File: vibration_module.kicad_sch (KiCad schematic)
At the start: 22 parts, among them J1 I2C/PWR, U1 AT42QT1011-TSHR, U2 DRV2605LDGS, U3 STM32G031G8Ux, U4 TPS7A20xxxDQN

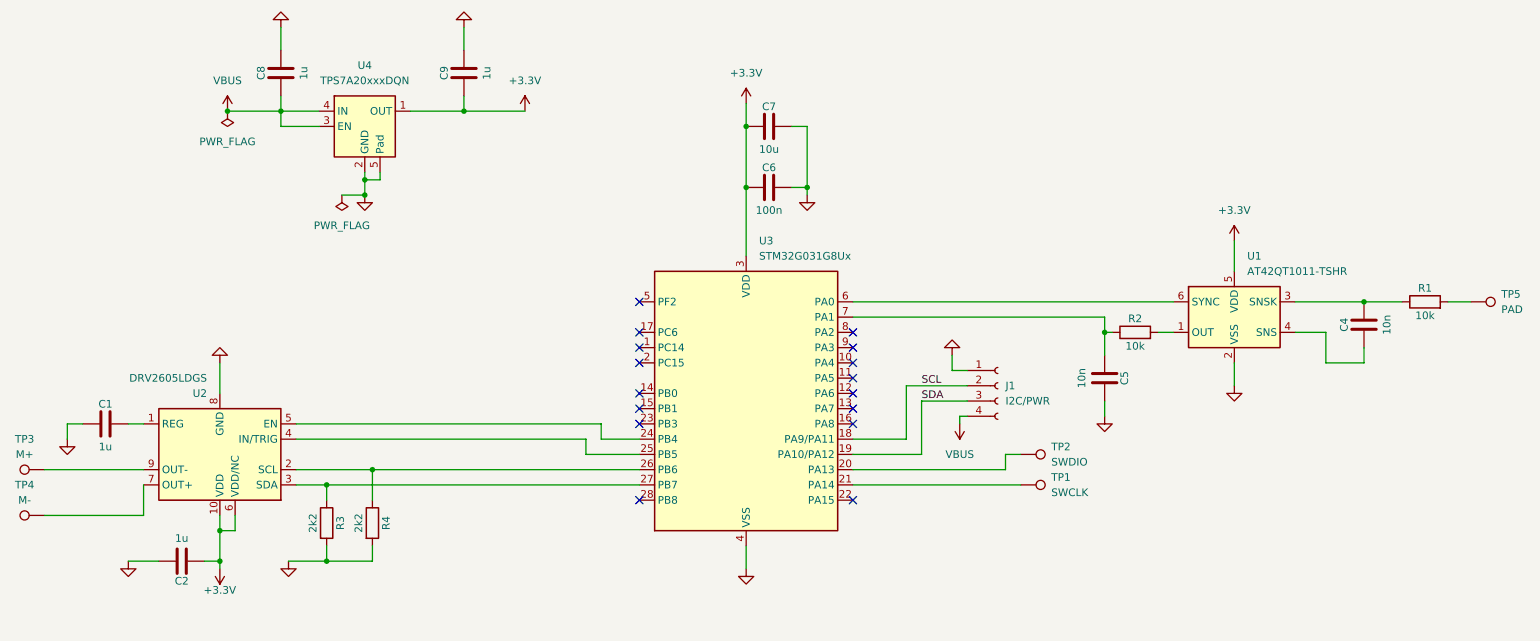
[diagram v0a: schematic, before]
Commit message: mouse switch integration
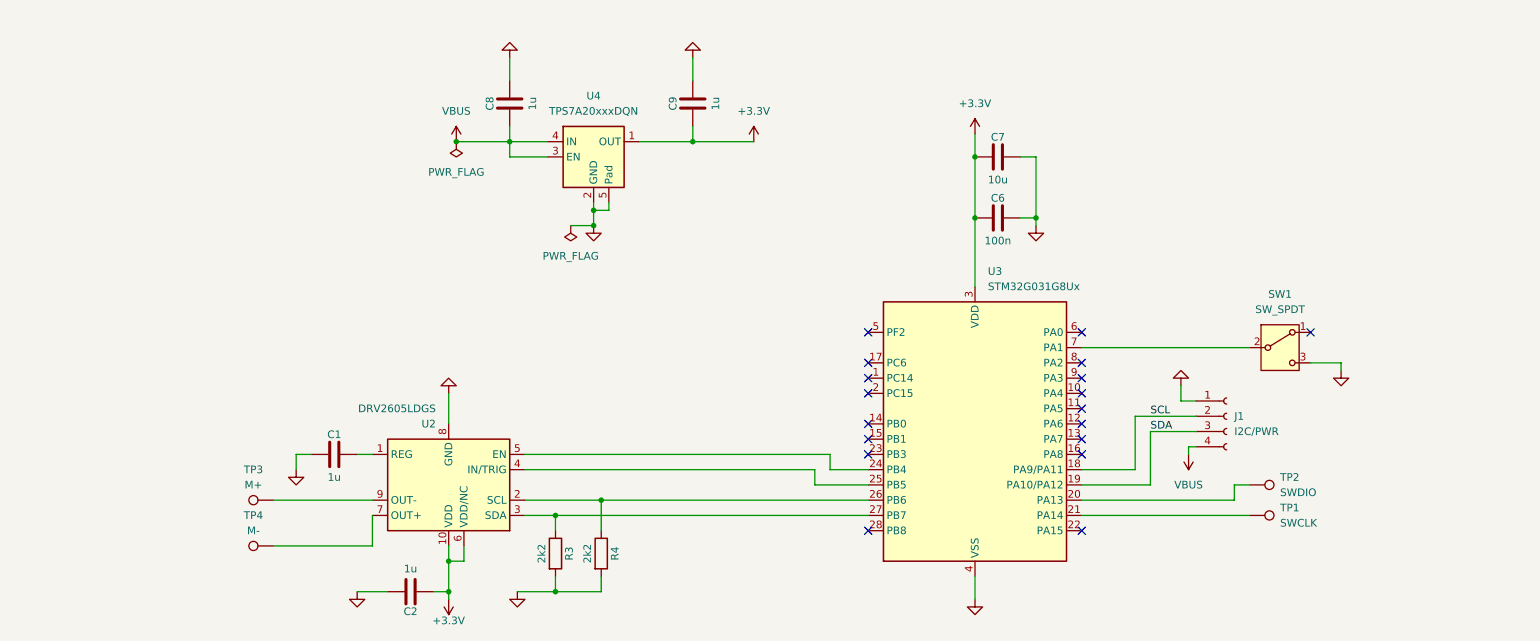
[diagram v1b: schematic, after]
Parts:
- removed C4, C5: 10n, Capacitor_SMD:C_0402_1005Metric, symbol Device:C
- removed R1, R2: 10k, Resistor_SMD:R_0402_1005Metric, symbol Device:R
- removed TP5: PAD, symbol Connector:TestPoint
- removed U1: AT42QT1011-TSHR, Package_TO_SOT_SMD:SOT-23-6, symbol Sensor_Touch:AT42QT1011-TSHR
- added SW1: SW_SPDT, Button_Switch_THT:SW_XKB_DM1-16UP-1, symbol Switch:SW_SPDT
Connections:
- net GND: now also SW1.3 (C)
- net at U3.7 (PA1): now also SW1.2 (B)
- no-connect marks 16 -> 18
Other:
- moved on the sheet: C1, C2, C6, C7, C8, C9, J1, R3, R4, TP1, TP2, TP3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

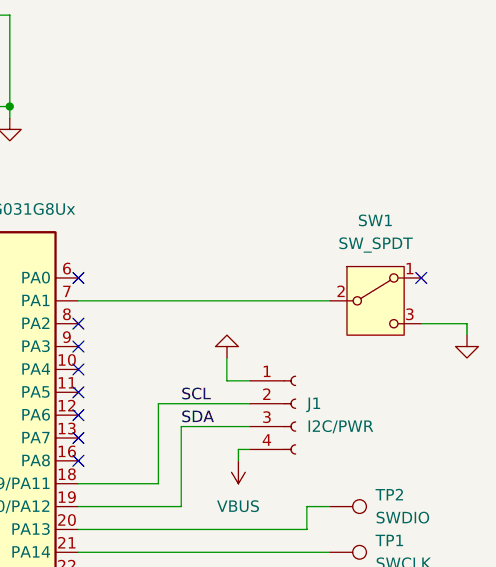
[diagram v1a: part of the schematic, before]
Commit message: keyboard version poc
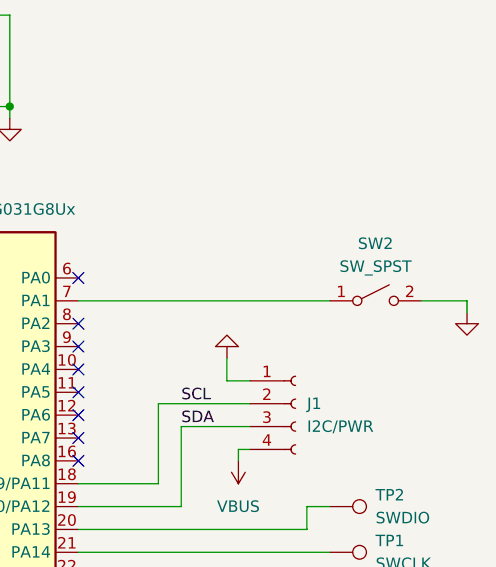
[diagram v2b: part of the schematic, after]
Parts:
- removed SW1: SW_SPDT, Button_Switch_THT:SW_XKB_DM1-16UP-1, symbol Switch:SW_SPDT
- added SW2: SW_SPST, PCM_Switch_Keyboard_Kailh:SW_Kailh_Choc_V1_1.00u, symbol Switch:SW_SPST
- J1: footprint Connector_Molex:Molex_PicoBlade_53048-0410_1x04_P1.25mm_Horizontal -> Connector_Molex:Molex_PicoBlade_53261-0471_1x04-1MP_P1.25mm_Horizontal
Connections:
- net GND: now also SW2.2 (B)
- net at U3.7 (PA1): now also SW2.1 (A)
- no-connect marks 18 -> 17
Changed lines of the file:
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@@
-	)
-	(no_connect
-		(at 240.03 101.6)
 	)
 	(no_connect
@@
 	(wire
 		(pts
-			(xy 240.03 106.68) (xy 245.11 106.68)
+			(xy 240.03 104.14) (xy 245.11 104.14)
 		)
 		(stroke
@@
 	(wire
 		(pts
-			(xy 245.11 106.68) (xy 245.11 107.95)
+			(xy 245.11 104.14) (xy 245.11 105.41)
 		)
 		(stroke
@@
 	)
 	(symbol
-		(lib_id "Switch:SW_SPDT")
-		(at 234.95 104.14 0)
-		(unit 1)
-		(exclude_from_sim no)
-		(in_bom yes)
-		(on_board yes)
-		(dnp no)
-		(fields_autoplaced yes)
-		(property "Reference" "SW1"
-			(at 234.95 95.25 0)
-			(effects
-				(font
-					(size 1.27 1.27)
-				)
-			)
-		)
-		(property "Value" "SW_SPDT"
-			(at 234.95 97.79 0)
-			(effects
-				(font
-					(size 1.27 1.27)
-				)
-			)
-		)
-		(property "Footprint" "Button_Switch_THT:SW_XKB_DM1-16UP-1"
-			(at 234.95 104.14 0)
-			(effects
-				(font
-					(size 1.27 1.27)
-				)
-				(hide yes)
-			)
-		)
-		(property "Datasheet" "~"
-			(at 234.95 111.76 0)
-			(effects
-				(font
-					(size 1.27 1.27)
-				)
-				(hide yes)
-			)
-		)
-		(property "Description" "Switch, single pole double throw"
-			(at 234.95 104.14 0)
-			(effects
-				(font
-					(size 1.27 1.27)
-				)
-				(hide yes)
-			)
-		)
-		(pin "2"
-		)
-		(pin "3"
-		)
-		(pin "1"
-		)
-		(instances
-			(project ""
-				(path "/b37f322b-8232-4f81-8199-988eec1c2a84"
-					(reference "SW1")
-					(unit 1)
-				)
-			)
-		)
-	)
-	(symbol
 		(lib_id "Device:C")
 		(at 77.47 121.92 90)
@@
 	)
 	(symbol
+		(lib_id "Switch:SW_SPST")
+		(at 234.95 104.14 0)
+		(unit 1)
+		(exclude_from_sim no)
+		(in_bom yes)
+		(on_board yes)
+		(dnp no)
+		(fields_autoplaced yes)
+		(property "Reference" "SW2"
+			(at 234.95 97.79 0)
+			(effects
+				(font
+					(size 1.27 1.27)
+				)
+			)
+		)
+		(property "Value" "SW_SPST"
+			(at 234.95 100.33 0)
+			(effects
+				(font
+					(size 1.27 1.27)
+				)
+			)
+		)
+		(property "Footprint" "PCM_Switch_Keyboard_Kailh:SW_Kailh_Choc_V1_1.00u"
+			(at 234.95 104.14 0)
+			(effects
+				(font
+					(size 1.27 1.27)
+				)
+				(hide yes)
+			)
+		)
+		(property "Datasheet" "~"
+			(at 234.95 104.14 0)
+			(effects
+				(font
+					(size 1.27 1.27)
+				)
+				(hide yes)
+			)
+		)
+		(property "Description" "Single Pole Single Throw (SPST) switch"
+			(at 234.95 104.14 0)
+			(effects
+				(font
+					(size 1.27 1.27)
+				)
+				(hide yes)
+			)
+		)
+		(pin "1"
+		)
+		(pin "2"
+		)
+		(instances
+			(project ""
+				(path "/b37f322b-8232-4f81-8199-988eec1c2a84"
+					(reference "SW2")
+					(unit 1)
+				)
+			)
+		)
+	)
+	(symbol
 		(lib_id "power:+3.3V")
 		(at 184.15 68.58 0)
@@
 	(symbol
 		(lib_id "power:GND")
-		(at 245.11 107.95 0)
+		(at 245.11 105.41 0)
 		(unit 1)
 		(exclude_from_sim no)
@@
 		(fields_autoplaced yes)
 		(property "Reference" "#PWR04"
-			(at 245.11 114.3 0)
+			(at 245.11 111.76 0)
 			(effects
 				(font
@@
 		)
 		(property "Value" "GND"
-			(at 245.11 113.03 0)
+			(at 245.11 110.49 0)
 			(effects
 				(font
@@
 		)
 		(property "Footprint" ""
-			(at 245.11 107.95 0)
+			(at 245.11 105.41 0)
 			(effects
 				(font
@@
 		)
 		(property "Datasheet" ""
-			(at 245.11 107.95 0)
+			(at 245.11 105.41 0)
 			(effects
 				(font
@@
 		)
 		(property "Description" "Power symbol creates a global label with name \"GND\" , ground"
-			(at 245.11 107.95 0)
+			(at 245.11 105.41 0)
 			(effects
 				(font
@@
 			)
 		)
-		(property "Footprint" "Connector_Molex:Molex_PicoBlade_53048-0410_1x04_P1.25mm_Horizontal"
+		(property "Footprint" "Connector_Molex:Molex_PicoBlade_53261-0471_1x04-1MP_P1.25mm_Horizontal"
 			(at 226.06 115.57 0)
 			(effects
